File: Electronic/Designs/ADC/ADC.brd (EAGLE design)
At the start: 50 x 50 mm, 36 parts

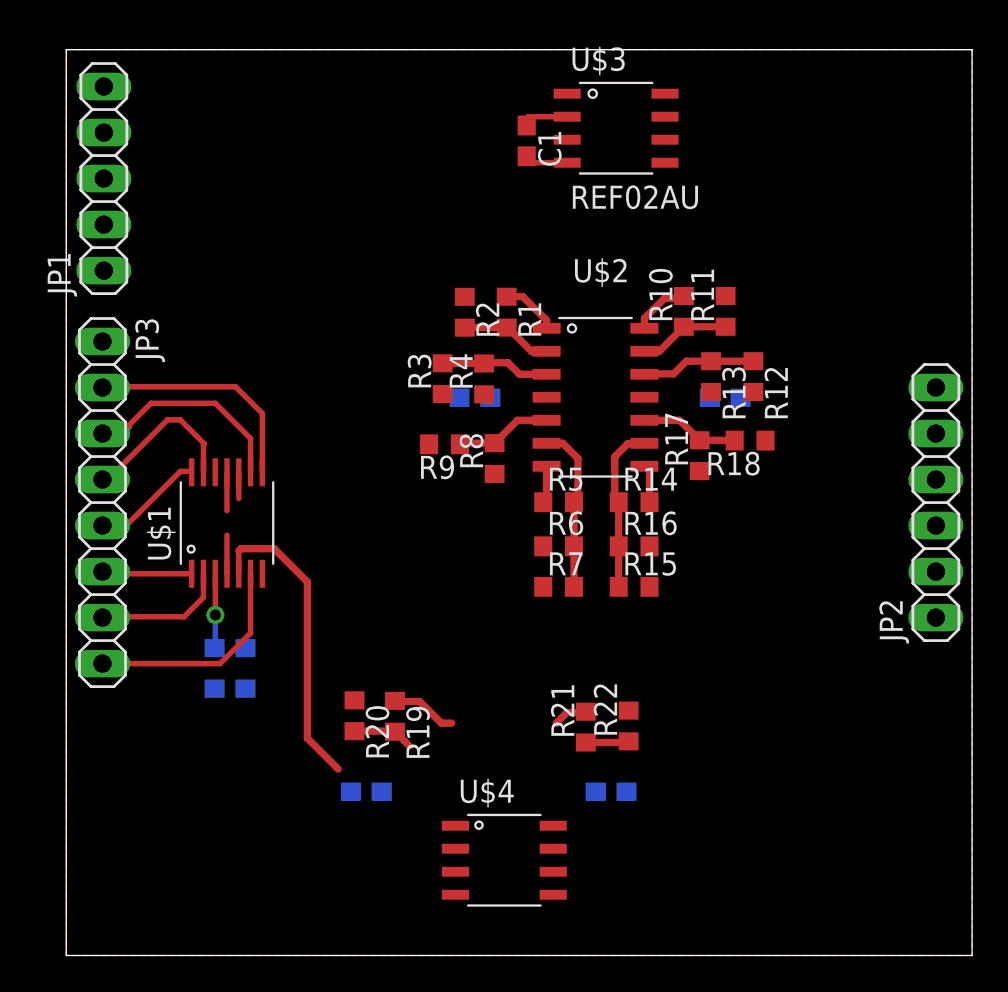
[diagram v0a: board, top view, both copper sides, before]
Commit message: Added ADC board and schematic
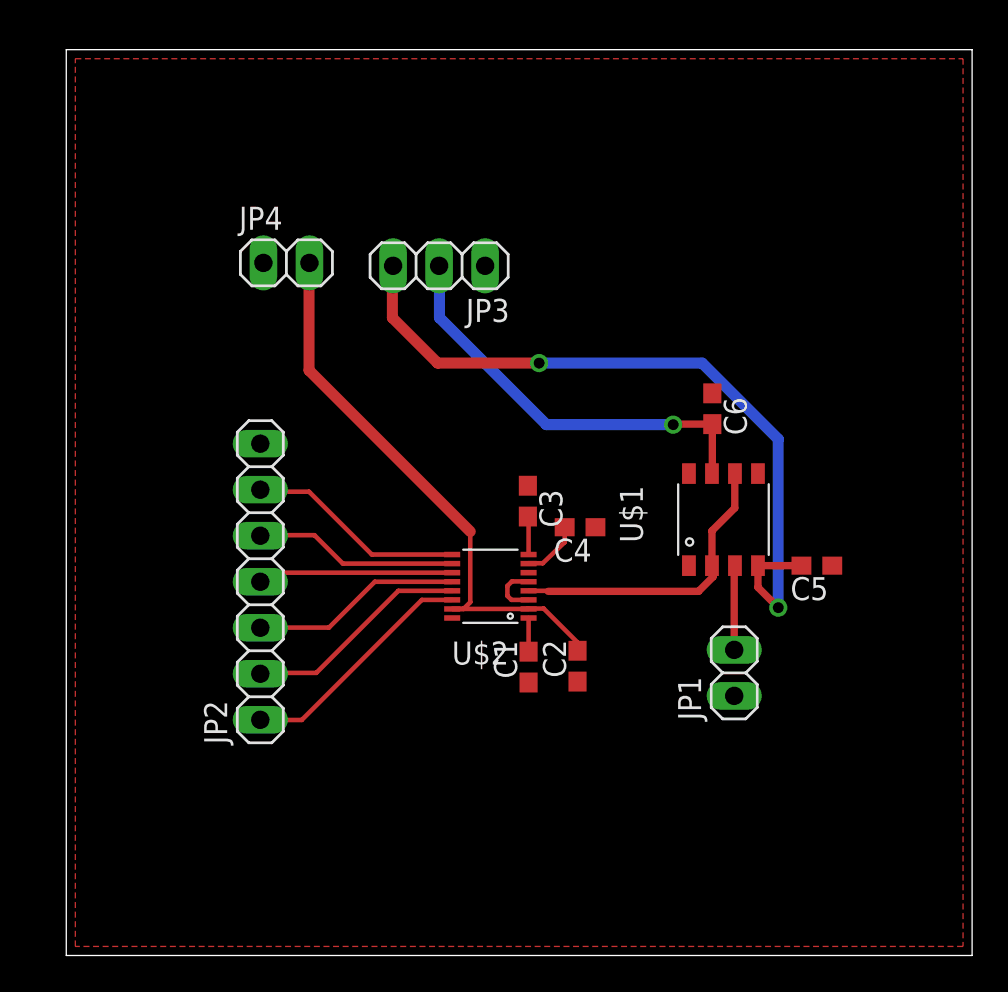
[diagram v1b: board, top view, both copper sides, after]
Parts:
- removed C7: 1uf, resistor:C0603
- removed R1, R10, R13, R14, R4, R5: 40k, resistor:R0603
- removed R11, R12, R18, R19, R2, R20, R21, R22, R3, R6, R7, R9: 10k, resistor:R0603
- removed R15, R16: 10K, resistor:R0603
- removed R17, R8: 8k, resistor:R0603
- removed U$3: REF02AU, REF02:SO8
- removed U$4: OPA2227UA, OPAX22X:SOIC-8
- added JP4: PW2, pinhead:1X02
- C1, C3: value 0.1uf -> 100nf
- C2, C5, C6: value 1uf -> 100nf
- C4: value 1uf -> 47uf
- JP1: value PWR -> AIN; device pinhead:1X05 -> pinhead:1X02
- JP2: value AOUT -> DOUT; device pinhead:1X06 -> pinhead:1X07
- JP3: value DIGITAL -> PW1; device pinhead:1X08 -> pinhead:1X03
- U$1: value DAC80004IPW -> LT1468; device DAC80004:TSSOP14 -> LT1468:SOIC-8
- U$2: value OPA4227UA -> LTC2326-16; device OPAX22X:SOIC-14 -> LTC2326-16:16-MSOP
- moved JP1 44.2 mm to (36.9, 15.6)
- moved JP2 37.5 mm to (10.7, 20.6)
- moved C1 29.0 mm to (25.5, 15.9), turned to 90 degrees
- moved U$1 26.8 mm to (35.6, 24.1)
- moved JP3 22.7 mm to (20.6, 38.1), turned to 180 degrees
- moved C6 21.9 mm to (35.7, 30.2), flipped to the top, turned to 270 degrees
- moved C5 21.0 mm to (41.4, 21.5), flipped to the top, turned to 180 degrees
- moved C3 19.4 mm to (25.5, 25.1), flipped to the top, turned to 270 degrees
- moved C2 19.2 mm to (28.2, 16.0), flipped to the top, turned to 90 degrees
- moved U$2 11.7 mm to (23.4, 20.6), turned to 180 degrees
- moved C4 10.7 mm to (28.4, 23.6), flipped to the top
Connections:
- removed net /CLR: JP3.3, U$1.P$9
- removed net /LDAC: JP3.6, U$1.P$1
- removed net /SYNC: JP3.7, U$1.P$2
- removed net B: U$1.P$5, U$4.P$3
- removed net BIAS: JP2.5, R21.2, U$4.P$7
- removed net N$14: R12.1, R13.1, U$2.P$12
- removed net N$15: R14.1, R15.1, R16.1, U$2.P$9
- removed net N$16: R10.1, R11.1, U$2.P$13
- removed net N$19: R19.2, R20.2, U$4.P$2
- removed net N$20: R17.2, R18.2, U$2.P$10
- removed net N$21: R19.1, U$4.P$1, U$4.P$5
- removed net N$22: R21.1, R22.1, U$4.P$6
- removed net N$4: R1.2, R2.2, U$2.P$2
- removed net N$6: R5.2, R6.2, R7.2, U$2.P$6
- removed net POR: JP3.8, U$1.P$6
- removed net SCLK: JP3.5, U$1.P$14
- removed net SDIN: JP3.4, U$1.P$13
- removed net VREF: R18.1, R20.1, R9.2, U$1.P$7, U$3.P$6
- removed net X: R3.1, R6.1, U$1.P$11
- removed net XNEG: JP2.2, R5.1, U$2.P$7
- removed net XPOS: JP2.1, R1.1, U$2.P$1
- removed net Y: R12.2, R15.2, U$1.P$10
- removed net YNEG: JP2.4, R14.2, U$2.P$8
- removed net YPOS: JP2.3, R10.2, U$2.P$14
- removed net Z: R11.2, R16.2, R2.1, R7.1, U$1.P$4
- new net BUSY: JP2.4, U$2.P11
- new net CHAIN: JP2.5, U$2.P10
- new net CNV: JP2.6, U$2.P9
- new net N$1: U$1.P$2, U$1.P$6, U$2.P4
- new net N$2: C4.2, U$2.P7
- new net N$3: C3.2, U$2.P8
- new net RDL/SDI: JP2.3, U$2.P12
- new net SCK: JP2.2, U$2.P13
- net +15V: now also C6.2, JP3.2, U$1.P$7; no longer C1.1, C4.1, C7.1, JP1.4, U$2.P$4, U$3.P$2, U$4.P$8
- net +5V: now also C2.2, JP4.2, U$2.P15, U$2.P2; no longer C2.1, C3.1, JP1.2, U$1.P$3
- net -15V: now also C5.2, JP3.3, U$1.P$4; no longer C5.1, C6.1, JP1.5, U$2.P$11, U$4.P$4
- net GND: now also C1.1, C2.1, C3.1, C4.1, C5.1, C6.1, JP2.7, JP4.1, U$2.P16, U$2.P3, U$2.P5, U$2.P6; no longer C1.2, C2.2, C3.2, C4.2, C5.2, C6.2, C7.2, JP1.3, JP2.6, R13.2, R17.1, R22.2, R4.1, R8.1, U$1.P$12, U$3.P$4
- net N$5: now also C1.2, U$2.P1; no longer R3.2, R4.2, U$2.P$3
- net N$7: now also JP1.2, U$1.P$3; no longer R8.2, R9.1, U$2.P$5
- net SDO: now also JP2.1, U$2.P14; no longer JP3.2, U$1.P$8
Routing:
- net -15V: track 0.00 -> 41.4 mm, vias 0 -> 2
- net +5V: track 3.89 -> 31.9 mm, vias 1 -> 0
- net +15V: track 2.65 -> 23.2 mm, vias 0 -> 1
- net B: track 16.9 -> 0.00 mm
- net N$1: track 0.00 -> 16.8 mm
- net SCK: track 0.00 -> 12.5 mm
- net POR: track 12.1 -> 0.00 mm
- net CNV: track 0.00 -> 12.1 mm
- net RDL/SDI: track 0.00 -> 11.6 mm
- net /CLR: track 11.6 -> 0.00 mm
- net CHAIN: track 0.00 -> 11.3 mm
- net BUSY: track 0.00 -> 10.8 mm
- net N$6: track 9.37 -> 0.00 mm
- net N$15: track 9.22 -> 0.00 mm
- net SDIN: track 9.17 -> 0.00 mm
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
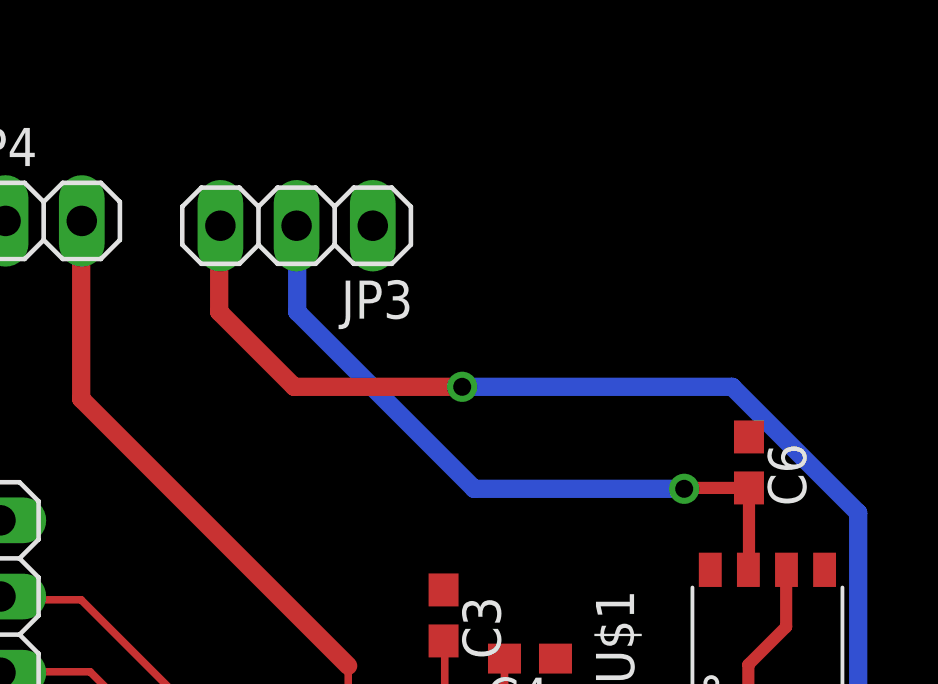
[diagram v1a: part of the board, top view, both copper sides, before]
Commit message: adjusted adc pwr pins on board
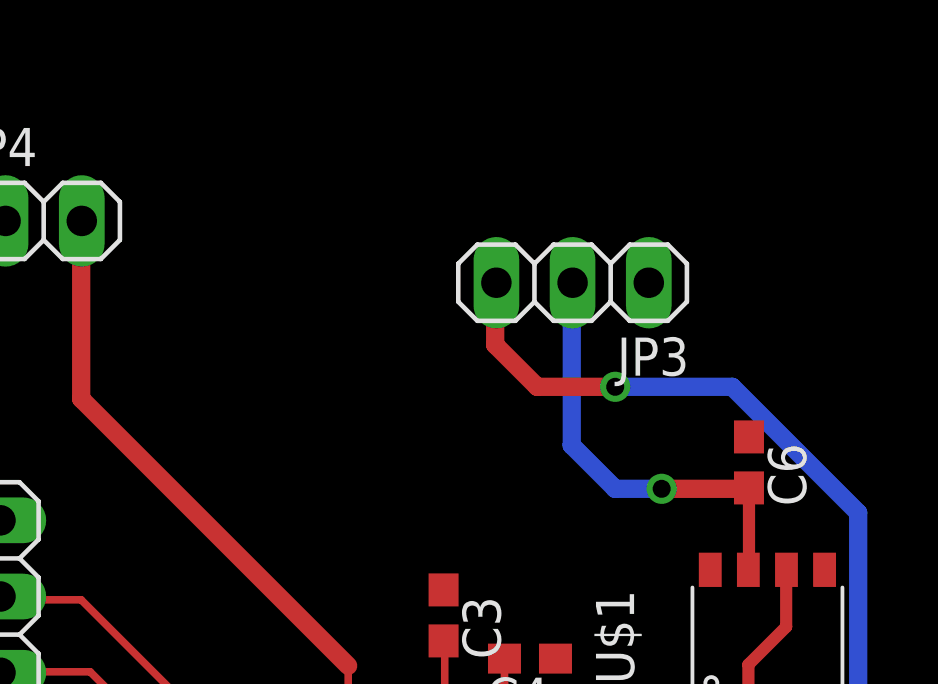
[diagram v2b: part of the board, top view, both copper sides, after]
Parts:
- moved JP3 9.39 mm to (29.8, 36.2)
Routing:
- net -15V: track 41.4 -> 31.0 mm
- net +15V: track 23.2 -> 14.7 mm
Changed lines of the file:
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@@
 <element name="JP1" library="pinhead" package="1X02" value="AIN" x="36.87" y="15.6" rot="R90"/>
 <element name="JP2" library="pinhead" package="1X07" value="DOUT" x="10.71" y="20.63" rot="R90"/>
-<element name="JP3" library="pinhead" package="1X03" value="PW1" x="20.58" y="38.07" rot="R180"/>
+<element name="JP3" library="pinhead" package="1X03" value="PW1" x="29.78" y="36.17" rot="R180"/>
 <element name="JP4" library="pinhead" package="1X02" value="PW2" x="12.15" y="38.23"/>
 <element name="U$1" library="LT1468" package="SOIC-8" value="LT1468" x="35.64" y="24.06" rot="R90"/>
@@
 <wire x1="39.3" y1="19.2" x2="39.3" y2="28.5" width="0.6096" layer="16"/>
 <wire x1="39.3" y1="28.5" x2="35.1" y2="32.7" width="0.6096" layer="16"/>
-<wire x1="35.1" y1="32.7" x2="26.1" y2="32.7" width="0.6096" layer="16"/>
-<via x="26.1" y="32.7" extent="1-16" drill="0.6"/>
-<wire x1="26.1" y1="32.7" x2="20.5" y2="32.7" width="0.6096" layer="1"/>
-<wire x1="20.5" y1="32.7" x2="18" y2="35.2" width="0.6096" layer="1"/>
-<wire x1="18" y1="35.2" x2="18" y2="38.03" width="0.6096" layer="1"/>
-<wire x1="18" y1="38.03" x2="18.04" y2="38.07" width="0.4064" layer="1"/>
+<wire x1="35.1" y1="32.7" x2="31.2" y2="32.7" width="0.6096" layer="16"/>
+<via x="31.2" y="32.7" extent="1-16" drill="0.6"/>
+<wire x1="31.2" y1="32.7" x2="28.6" y2="32.7" width="0.6096" layer="1"/>
+<wire x1="28.6" y1="32.7" x2="27.2" y2="34.1" width="0.6096" layer="1"/>
+<wire x1="27.2" y1="34.1" x2="27.2" y2="36.13" width="0.6096" layer="1"/>
+<wire x1="27.2" y1="36.13" x2="27.24" y2="36.17" width="0.4064" layer="1"/>
 </signal>
 <signal name="+15V">
@@
 <wire x1="35.66" y1="29.33" x2="35.66" y2="26.62" width="0.4064" layer="1"/>
 <wire x1="35.66" y1="26.62" x2="35.64" y2="26.6" width="0.4064" layer="1"/>
-<wire x1="20.6" y1="38.05" x2="20.58" y2="38.07" width="0.4064" layer="1"/>
-<wire x1="35.66" y1="29.33" x2="33.53" y2="29.33" width="0.4064" layer="1"/>
-<wire x1="33.53" y1="29.33" x2="33.5" y2="29.3" width="0.4064" layer="1"/>
-<via x="33.5" y="29.3" extent="1-16" drill="0.6"/>
-<wire x1="33.5" y1="29.3" x2="26.5" y2="29.3" width="0.6096" layer="16"/>
-<wire x1="26.5" y1="29.3" x2="20.6" y2="35.2" width="0.6096" layer="16"/>
-<wire x1="20.6" y1="35.2" x2="20.6" y2="38.05" width="0.6096" layer="16"/>
-<wire x1="20.6" y1="38.05" x2="20.58" y2="38.07" width="0.4064" layer="16"/>
+<via x="32.75" y="29.3" extent="1-16" drill="0.6"/>
+<wire x1="32.75" y1="29.3" x2="31.2" y2="29.3" width="0.6096" layer="16"/>
+<wire x1="31.2" y1="29.3" x2="29.75" y2="30.75" width="0.6096" layer="16"/>
+<wire x1="29.75" y1="30.75" x2="29.75" y2="36.14" width="0.6096" layer="16"/>
+<wire x1="29.75" y1="36.14" x2="29.78" y2="36.17" width="0.4064" layer="16"/>
+<wire x1="32.75" y1="29.3" x2="35.63" y2="29.3" width="0.6096" layer="1"/>
+<wire x1="35.63" y1="29.3" x2="35.66" y2="29.33" width="0.6096" layer="1"/>
 </signal>
 <signal name="N$2">
